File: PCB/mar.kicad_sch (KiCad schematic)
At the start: 19 parts, among them SW3 SW_DIP_x04, SW4 SW_SPDT, U18 74LS157, U19 74LS173

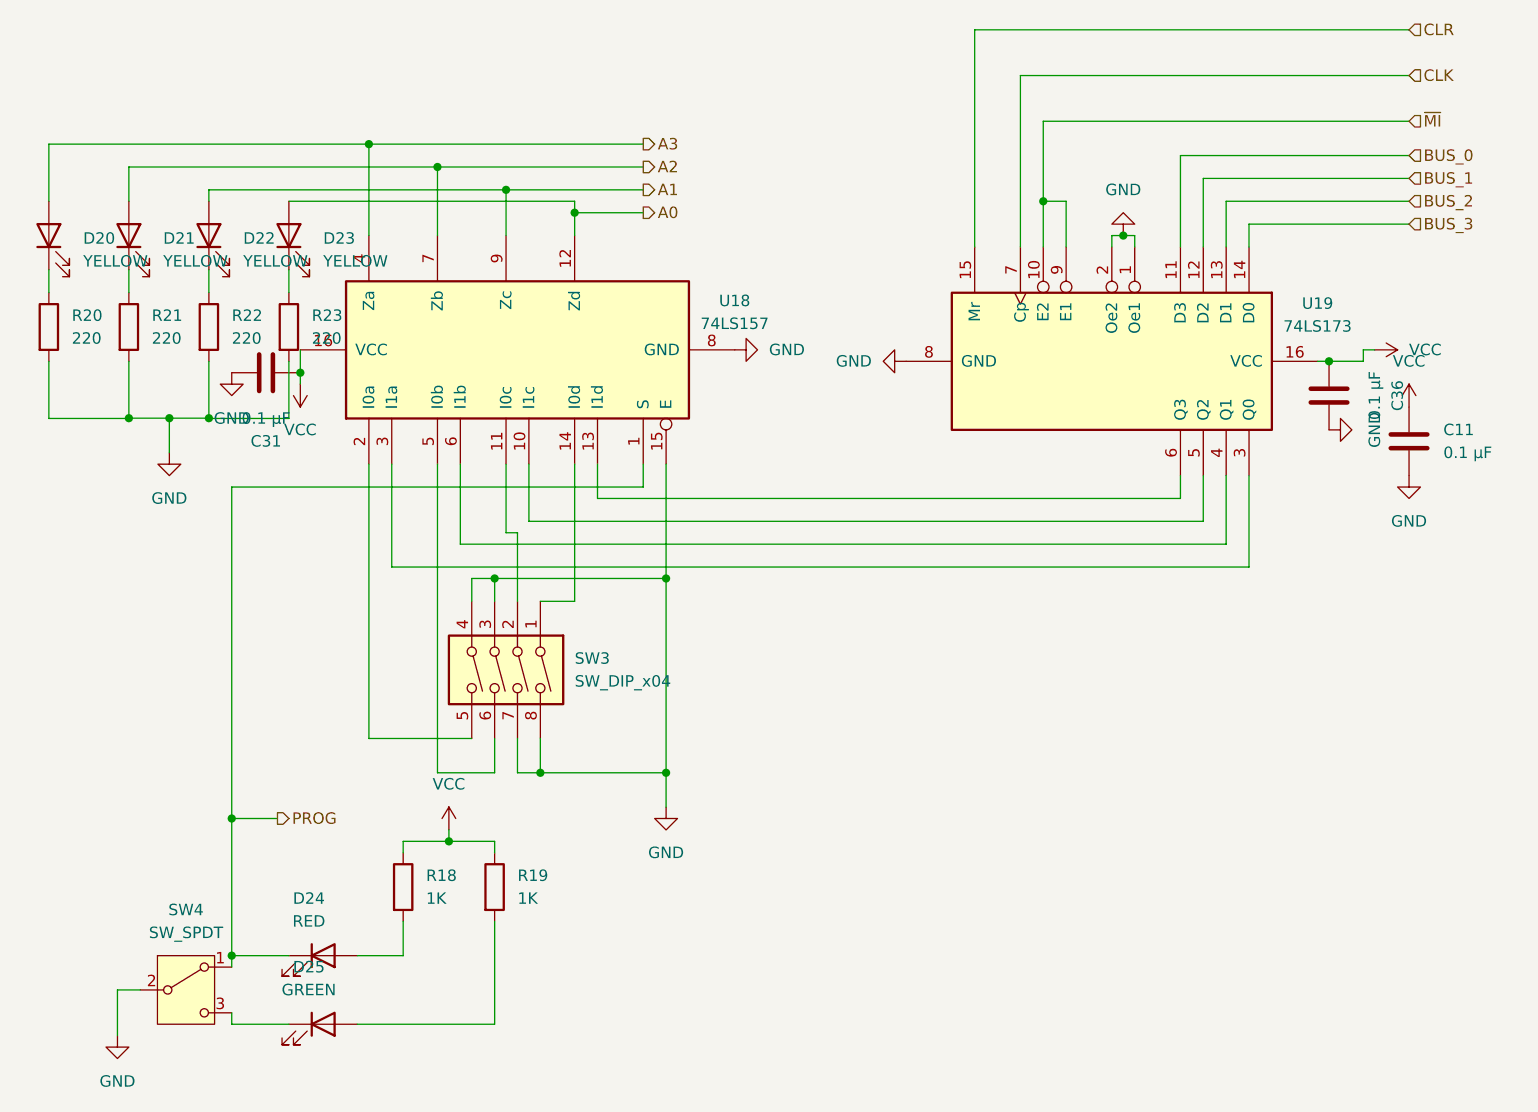
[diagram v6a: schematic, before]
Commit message: Redoing PCB layout and fixed some signal flow convention errors
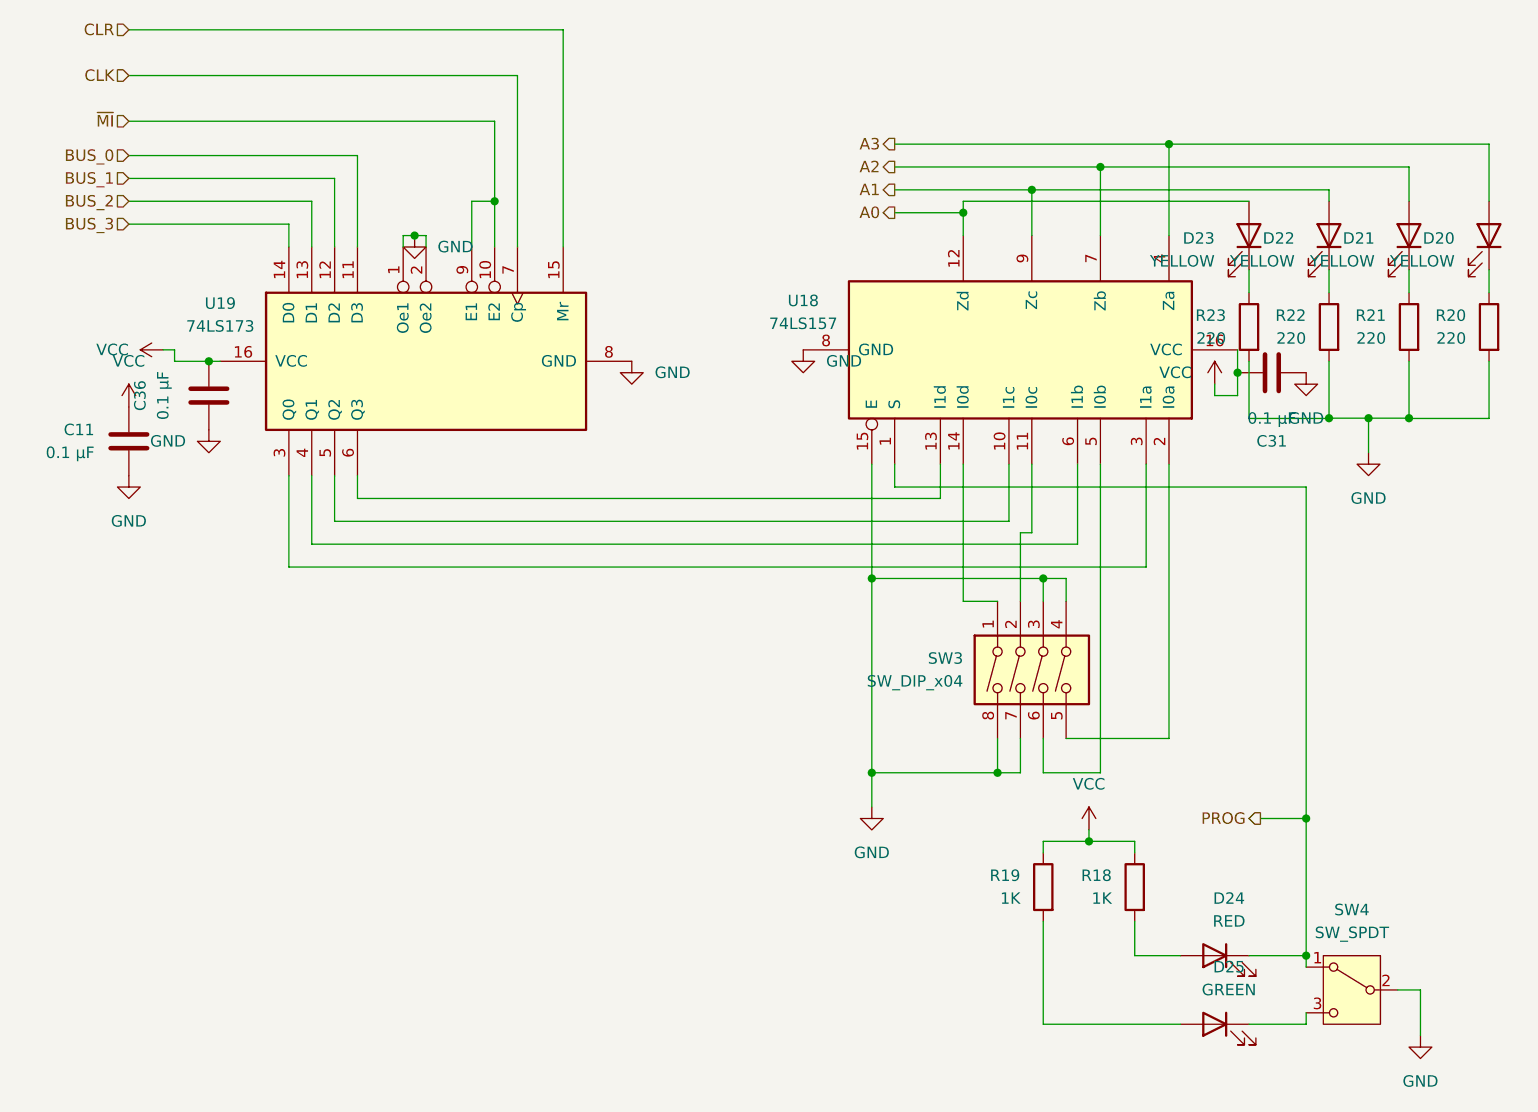
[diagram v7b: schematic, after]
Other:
- moved on the sheet: C11, C31, C36, D20, D21, D22, D23, D24, D25, R18, R19, R20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

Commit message: update BOM to reflect cheaper prices and more acurate item ammounts, also worked on laying out the PCB.
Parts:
- SW4: footprint Button_Switch_SMD:SW_SPDT_CK_JS102011SAQN -> Button_Switch_THT:SW_Slide-03_Wuerth-WS-SLTV_10x2.5x6.4_P2.54mm
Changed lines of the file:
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@@
 			)
 		)
-		(property "Footprint" "Button_Switch_SMD:SW_SPDT_CK_JS102011SAQN"
+		(property "Footprint" "Button_Switch_THT:SW_Slide-03_Wuerth-WS-SLTV_10x2.5x6.4_P2.54mm"
 			(at 161.29 121.92 0)
 			(effects
